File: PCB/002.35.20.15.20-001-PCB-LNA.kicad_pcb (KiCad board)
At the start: 2 copper layers, 86.4 x 49.4 mm, 29 parts, among them J1 Conn_Coaxial, J2 Conn_Coaxial, J3 Conn_Coaxial, U1 PMA2-63LN+, U2 PMA2-63LN+, U3 YAT-1A+, U4 L7805, U5 L7805

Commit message: Added board comments and assembly plot
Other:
- board text added: "Notes: LNA footprint is pin-compatible with PMA2-123LN+. Board oscillates at ~10.5 GHz, cause unknown. Poor return loss - SMA pads not matched."
- board text removed: "LNA footprint is also pin-compatible with: PMA2-123LN+ PMA2-153LN+"
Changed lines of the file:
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@@
     (effects (font (size 1.5 1.5) (thickness 0.3) bold) (justify left bottom))
   )
-  (gr_text "LNA footprint is also pin-compatible with:\nPMA2-123LN+\nPMA2-153LN+" (at 177.8 167.005) (layer "Cmts.User")
+  (gr_text "Notes:\nLNA footprint is pin-compatible with PMA2-123LN+.\nBoard oscillates at ~10.5 GHz, cause unknown.\nPoor return loss - SMA pads not matched.\n" (at 177.8 167.005) (layer "Cmts.User")
     (effects (font (size 1.5 1.5) (thickness 0.3) bold) (justify left top))
   )

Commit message: Fixed SMA pad thickness
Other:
- board text added: "0"
- board text added: "0 mm"
- board text added: "0.0037"
- board text added: "0.01 mm"
- board text added: "0.03556 mm"
- board text added: "0.762 mm"
- board text added: "1"
- board text added: "3.3"
- board text added: "3.66"
- board text added: "B.Cu"
- board text added: "B.Mask"
- board text added: "B.Paste"
- board text added: "B.Silkscreen"
- board text added: "Bottom Silk Screen"
- board text added: "Bottom Solder Mask"
- board text added: "Bottom Solder Paste"
- board text added: "Color"
- board text added: "Dielectric 1"
- board text added: "Epsilon R"
- board text added: "F.Cu"
- board text added: "F.Mask"
- board text added: "F.Paste"
- board text added: "F.Silkscreen"
- board text added: "FR4 natural"
- board text added: "Green"
- board text added: "Layer Name"
- board text added: "Liquid Ink"
- board text added: "Liquid Photo"
- board text added: "Loss Tangent"
- board text added: "Material"
- board text added: "Notes: LNA footprint is pin-compatible with PMA2-123LN+."
- board text added: "RO4350B"
- board text added: "Thickness (mm)"
- board text added: "Top Silk Screen"
- board text added: "Top Solder Mask"
- board text added: "Top Solder Paste"
- board text added: "Type"
- board text added: "White"
- board text added: "copper"
- board text added: "core"
- board text removed: "Notes: LNA footprint is pin-compatible with PMA2-123LN+. Board oscillates at ~10.5 GHz, cause unknown. Poor return loss - SMA pads not matched."

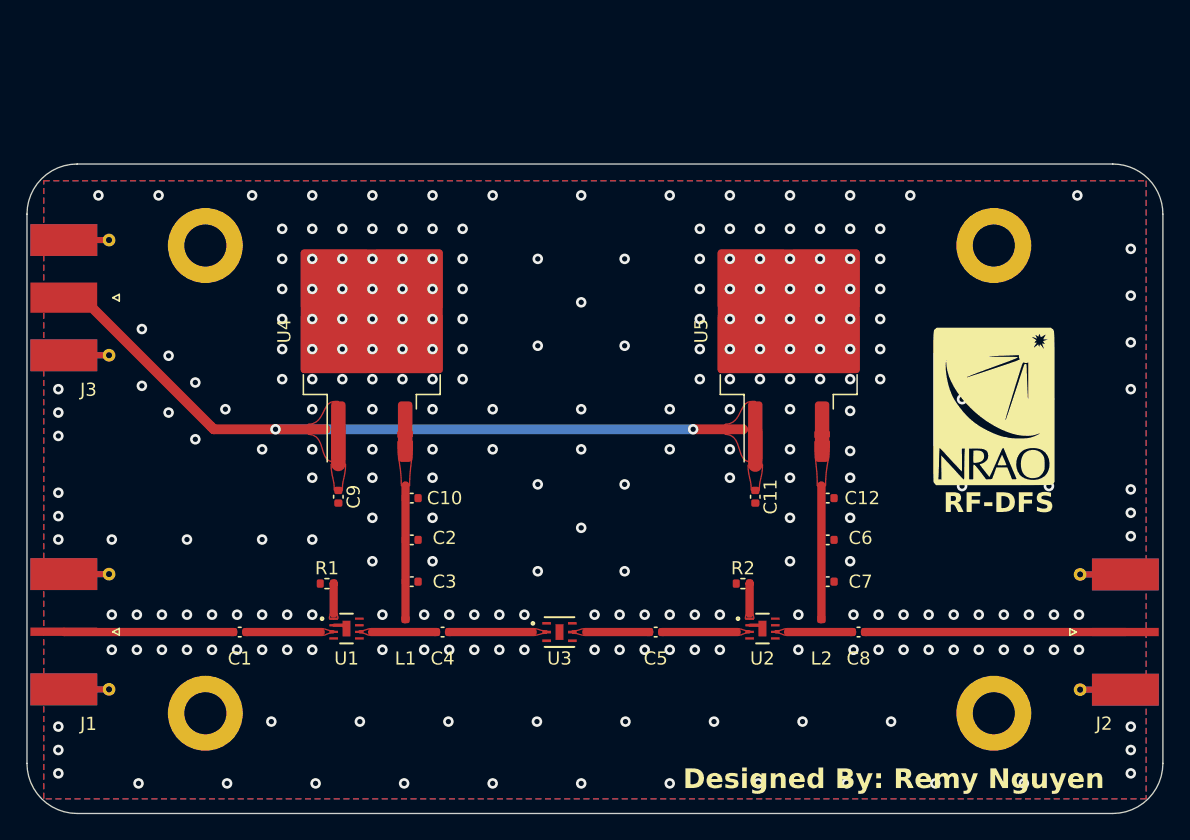
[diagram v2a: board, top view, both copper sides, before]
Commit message: PCB Rev B complete: compacted board and fixed sma pads
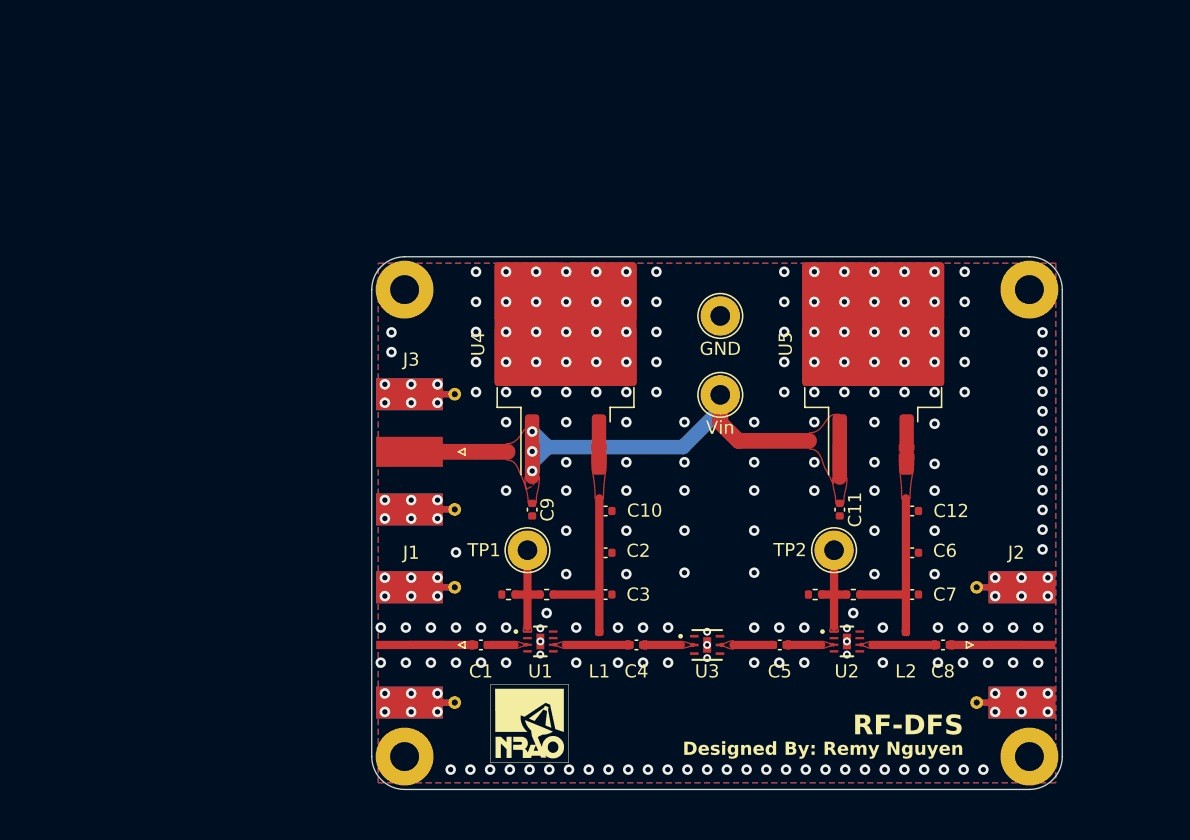
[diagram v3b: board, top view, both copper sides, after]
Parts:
- removed the G*** at (166.2, 93.3)
- removed the REF** at (166.2, 81.1)
- removed the REF** at (106.3, 116.7)
- removed the REF** at (106.3, 81.1)
- removed the REF** at (166.2, 116.7)
- added G***: LOGO, footprints.pretty:nrao1_6mm_silk, F.Cu at (130.9, 117.5)
- added GND: GND, TestPoint:TestPoint_Loop_D2.54mm_Drill1.5mm_Beaded, F.Cu at (145.4, 86.5)
- added R3: 100k, Resistor_SMD:R_0402_1005Metric, F.Cu at (132.2, 107.7)
- added R4: 100k, Resistor_SMD:R_0402_1005Metric, F.Cu at (155.5, 107.7)
- added REF**: 2.2mm M2, MountingHole:MountingHole_2.2mm_M2_Pad, F.Cu at (121.4, 84.5)
- added REF**: 2.2mm M2, MountingHole:MountingHole_2.2mm_M2_Pad, F.Cu at (168.9, 120.0)
- added REF**: 2.2mm M2, MountingHole:MountingHole_2.2mm_M2_Pad, F.Cu at (168.9, 84.5)
- added REF**: 2.2mm M2, MountingHole:MountingHole_2.2mm_M2_Pad, F.Cu at (121.4, 120.0)
- added TP1: TestPoint, TestPoint:TestPoint_Loop_D2.54mm_Drill1.5mm_Beaded, F.Cu at (130.8, 104.3)
- added TP2: TestPoint, TestPoint:TestPoint_Loop_D2.54mm_Drill1.5mm_Beaded, F.Cu at (154.1, 104.3)
- added Vin: Vin, TestPoint:TestPoint_Loop_D2.54mm_Drill1.5mm_Beaded, F.Cu at (145.4, 92.5)
- moved J3 28.8 mm to (123.5, 96.8)
- moved J1 26.3 mm to (123.5, 111.5)
- moved C1 18.4 mm to (127.2, 111.5)
- moved C10 14.8 mm to (136.7, 101.3)
- moved C2 14.8 mm to (136.7, 104.5)
- moved C3 14.8 mm to (136.7, 107.7)
- moved C4 14.8 mm to (139.0, 111.5)
- moved C9 14.8 mm to (131.1, 101.2)
- moved L1 14.8 mm to (136.2, 111.0)
- moved U4 14.8 mm to (133.7, 88.6)
- moved U1 14.8 mm to (131.7, 111.2)
- moved R1 13.8 mm to (129.3, 107.7)
- moved U3 11.3 mm to (144.4, 111.5)
- moved C5 9.48 mm to (149.9, 111.5)
- moved J2 7.93 mm to (166.6, 111.5)
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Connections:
- C1 pad 1: /LNA Biasing/LNA-IN -> /LNA Biasing1/LNA-IN
- C4 pad 2: /LNA Biasing/LNA-OUT -> /LNA Biasing1/LNA-OUT
- C5 pad 1: /LNA Biasing1/LNA-IN -> /LNA Biasing2/LNA-IN
- C8 pad 2: /LNA Biasing1/LNA-OUT -> /LNA Biasing2/LNA-OUT
- J1 pad 1: /LNA Biasing/LNA-IN -> /LNA Biasing1/LNA-IN
- J2 pad 1: /LNA Biasing1/LNA-OUT -> /LNA Biasing2/LNA-OUT
- U3 pad 2: /LNA Biasing/LNA-OUT -> /LNA Biasing1/LNA-OUT
- U3 pad 5: /LNA Biasing1/LNA-IN -> /LNA Biasing2/LNA-IN
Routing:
- net Vin: track 64.6 -> 43.7 mm, vias 2 -> 3
- net /LNA Biasing1/LNA-OUT: track 19.8 -> 2.60 mm
- net /LNA Biasing/LNA-IN: track 12.9 -> 0.00 mm
- net /LNA Biasing/LNA-OUT: track 6.37 -> 0.00 mm
- net Net-(U1-LADJ): track 2.29 -> 7.69 mm
- net Net-(U2-LADJ): track 2.29 -> 7.69 mm
- net /LNA Biasing2/LNA-OUT: track 0.00 -> 5.23 mm
- net Net-(U1-RF-IN): track 5.68 -> 1.86 mm
- net Vdd1: track 10.2 -> 13.7 mm
- net Vdd2: track 10.2 -> 13.7 mm
- net Net-(U2-RF-IN): track 5.68 -> 2.37 mm
- net /LNA Biasing2/LNA-IN: track 0.00 -> 3.00 mm
- net GND: track 2.16 -> 0.00 mm, vias 259 -> 233
- added copper zone on F.Cu, net /LNA Biasing1/LNA-OUT
- added copper zone on F.Cu, net /LNA Biasing2/LNA-IN
- added copper zone on F.Cu, net /LNA Biasing2/LNA-OUT
- removed copper zone on F.Cu, net /LNA Biasing/LNA-OUT
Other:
- board size 86.4 x 49.4 mm -> 52.5 x 40.5 mm
- board text added: "4 x Ø2.20"
- board text added: "B"
- board text added: "M2"
- board text removed: "A"

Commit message: Updated board for Oshpark specifications
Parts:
- added G***: LOGO, imports:RF-DFS-GCPW-OSH, F.Cu at (239.0, 114.0)
- moved C10 25.3 mm to (117.0, 85.5)
- moved C12 25.3 mm to (140.3, 85.5)
- moved C2 25.3 mm to (117.0, 88.7)
- moved C3 25.3 mm to (117.0, 91.9)
- moved C5 25.3 mm to (130.2, 95.7)
- moved C6 25.3 mm to (140.3, 88.7)
- moved C7 25.3 mm to (140.3, 91.9)
- moved J2 25.3 mm to (146.9, 95.7)
- moved R2 25.3 mm to (132.9, 91.9)
- moved R3 25.3 mm to (112.5, 91.9)
- moved R4 25.3 mm to (135.8, 91.9)
- moved U2 25.3 mm to (135.3, 95.4)
- moved C1 25.3 mm to (107.5, 95.7)
- moved C4 25.3 mm to (119.3, 95.7)
- moved C9 25.3 mm to (111.4, 85.4)
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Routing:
- net Net-(U2-LADJ): track 7.69 -> 7.10 mm
- net Net-(U1-LADJ): track 7.69 -> 7.11 mm
- net GND: vias 233 -> 235
- added copper zone on In1.Cu, net GND
- added copper zone on In2.Cu, net GND
- removed copper zone on F.Cu, net /LNA Biasing1/LNA-IN
- removed copper zone on F.Cu, net /LNA Biasing2/LNA-OUT
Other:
- copper layers 2 -> 4
- board text added: "0.0000 mm / 0.0000 mm"
- board text added: "0.0098"
- board text added: "0.01"
- board text added: "0.0175 mm"
- board text added: "0.0254 mm"
- board text added: "0.0432 mm"
- board text added: "0.2021 mm"
- board text added: "0.3000 mm"
- board text added: "0.9906 mm"
- board text added: "1.5670 mm"
- board text added: "1/23/2024"
- board text added: "3.6"
- board text added: "3.64"
- board text added: "4"
- board text added: "52.5000 mm x 40.5000 mm"
- board text added: "BOARD CHARACTERISTICS"
- board text added: "BOT-L4"
- board text added: "Board Thickness:"
- board text added: "Board overall dimensions:"
- board text added: "Castellated pads:"
- board text added: "Copper Finish:"
- board text added: "Copper Layer Count:"
- board text added: "Dielectric 2"
- board text added: "Dielectric 3"
- board text added: "ENIG"
- board text added: "Edge card connectors:"
- board text added: "FR408-HR"
- board text added: "FR408HR 2113"
- board text added: "IN-L2"
- board text added: "IN-L3"
- board text added: "Impedance Control:"
- board text added: "In1.Cu"
- board text added: "In2.Cu"
- board text added: "Min hole diameter:"
- board text added: "Min track/spacing:"
- board text added: "No"
- board text added: "Plated Board Edge:"
- board text added: "Purple"
- board text added: "TOP-L1"
- board text added: "Yes"
- board text added: "prepreg"
- board text removed: "0.0037"
- board text removed: "0.01 mm"
- board text removed: "0.03556 mm"
- board text removed: "0.762 mm"
- board text removed: "3.66"
- board text removed: "7/6/2023"
- board text removed: "Green"
- board text removed: "RO4350B"

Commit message: Removed back mask from thermal pad and adjusted trace sizes for more accurate z0
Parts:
- moved G*** 1.96 mm to (237.1, 113.5)

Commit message: Minor updates to trace width, zone clearance, silkscreen
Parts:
- moved C11 2.73 mm to (136.6, 83.3)
- moved C9 2.73 mm to (113.2, 83.3)
- moved C12 2.44 mm to (142.1, 83.8)
- moved C6 2.44 mm to (142.1, 87.0)
- moved C7 2.44 mm to (142.1, 90.2)
- moved R2 2.44 mm to (134.7, 90.2)
- moved R4 2.44 mm to (137.6, 90.2)
- moved U5 2.44 mm to (139.1, 71.1)
- moved C5 2.44 mm to (132.0, 94.0)
- moved L2 2.44 mm to (141.6, 93.5)
- moved RF-Out 2.44 mm to (148.7, 94.0)
- moved U2 2.44 mm to (137.1, 93.8)
- moved C10 2.44 mm to (118.8, 83.8)
- moved C2 2.44 mm to (118.8, 87.0)
- moved C3 2.44 mm to (118.8, 90.2)
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- renumbered TP2 to Iadj, TP1 to Iadj, J1 to RF-In, J2 to RF-Out, J3 to Vin
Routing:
- net GND: vias 235 -> 234

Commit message: PCB Rev C Complete
* Landing pads improved with testing from Tx-Line boards
* Mounting holes correctly set to GND net
* Assembly drawing includes SMA connectors
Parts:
- moved C8 0.47 mm to (144.9, 94.0)
- moved RF-In 0.20 mm to (105.8, 94.0)
- moved Vin 0.20 mm to (105.8, 79.3)
- moved C1 0.10 mm to (109.4, 94.0)
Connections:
- REF** pad 1: (no net) -> GND (x4)
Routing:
- net GND: vias 234 -> 236
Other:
- board text added: "0.415 mm / 0.300 mm"
- board text added: "C"
- board text removed: "0.0000 mm / 0.0000 mm"
- board text removed: "B"

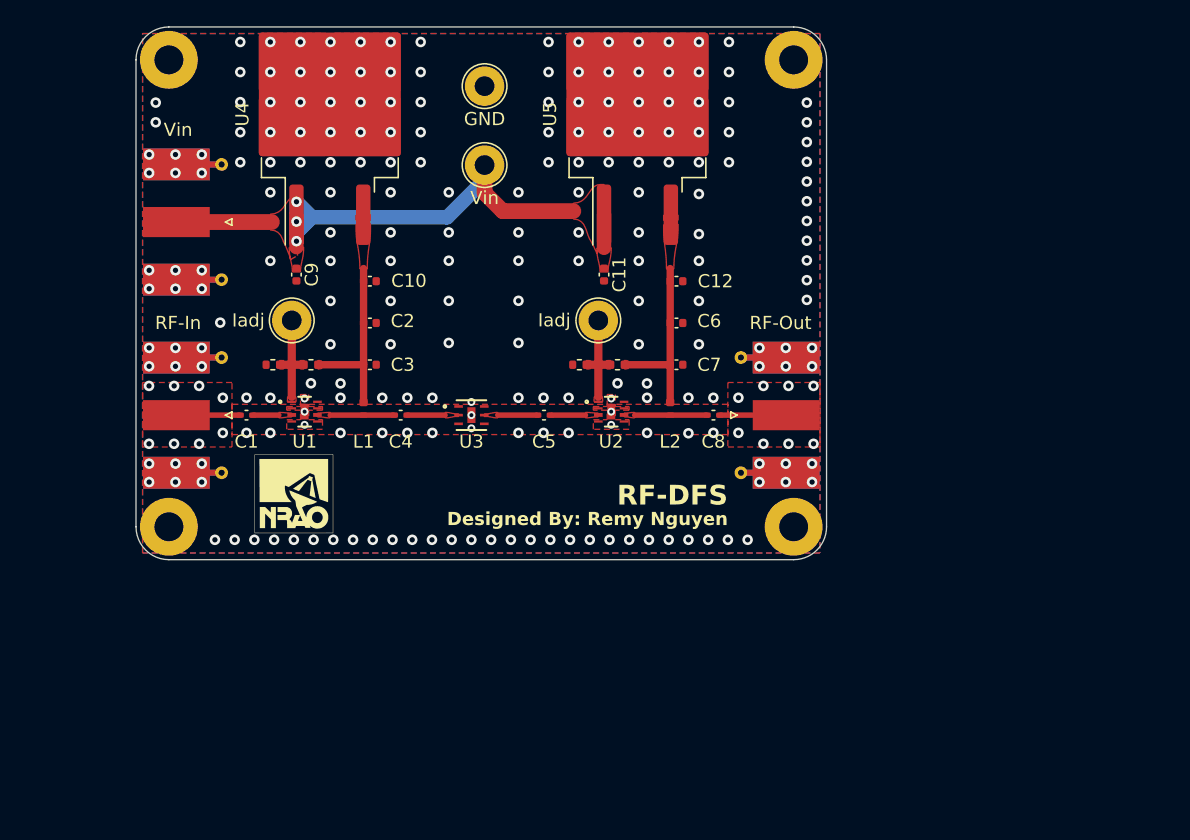
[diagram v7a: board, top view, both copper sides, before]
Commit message: Drawing sheets updated
* A4 --> Letter
* SMA connector diameter dimensioned
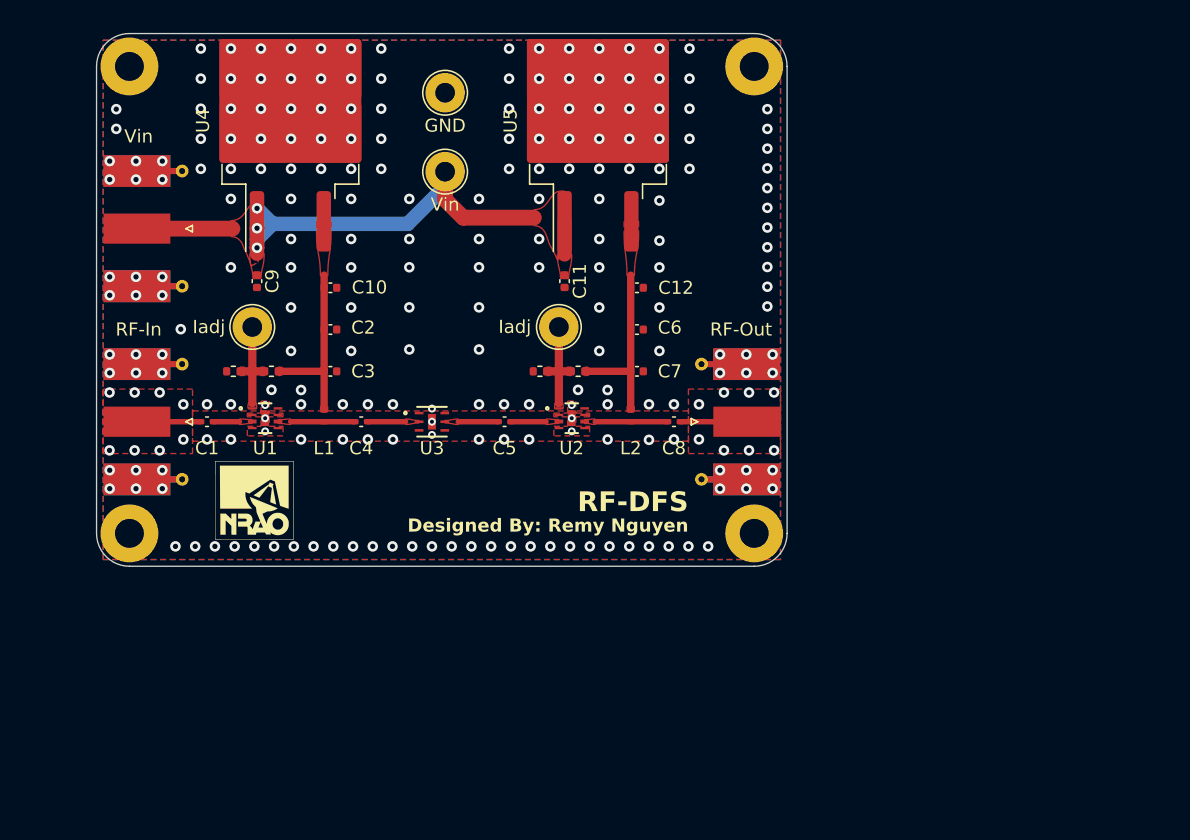
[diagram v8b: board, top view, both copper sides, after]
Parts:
- moved G*** 23.3 mm to (214.0, 118.0)
- moved C1 3.04 mm to (106.4, 94.5)
- moved C10 3.04 mm to (115.8, 84.3)
- moved C11 3.04 mm to (133.6, 83.8)
- moved C12 3.04 mm to (139.1, 84.3)
- moved C2 3.04 mm to (115.8, 87.5)
- moved C3 3.04 mm to (115.8, 90.7)
- moved C4 3.04 mm to (118.1, 94.5)
- moved C5 3.04 mm to (129.0, 94.5)
- moved C6 3.04 mm to (139.1, 87.5)
- moved C7 3.04 mm to (139.1, 90.7)
- moved C8 3.04 mm to (141.9, 94.5)
- moved C9 3.04 mm to (110.2, 83.8)
- moved G*** 3.04 mm to (110.0, 100.5)
- moved GND 3.04 mm to (124.5, 69.5)
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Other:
- board text added: "2/23/2024"
- board text added: "3 x Ø6.35"
- board text removed: "1/23/2024"
